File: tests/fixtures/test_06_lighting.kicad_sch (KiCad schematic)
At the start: 2 parts

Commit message: updated test 06 fixtures with LocLoad field
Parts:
- L1: CInfo |(0,0,100)L2.4 -> (none); LocLoad (none) -> (0,0,100)L2.4
- L2: CInfo |(0,0,-100)L2.4 -> (none); LocLoad (none) -> (0,0,-100)L2.4
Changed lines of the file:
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@@
 			)
 		)
-		(property "CInfo" "|(0,0,-100)L2.4"
+		(property "LocLoad" "(0,0,-100)L2.4"
 			(at 45.72 74.93 0)
 			(effects
@@
 			)
 		)
-		(property "CInfo" "|(0,0,10)G"
+		(property "LocLoad" "(0,0,10)G"
 			(at 62.23 74.93 0)
 			(effects
@@
 			)
 		)
-		(property "CInfo" "|(0,0,100)L2.4"
+		(property "LocLoad" "(0,0,100)L2.4"
 			(at 46.99 36.83 0)
 			(effects
@@
 			)
 		)
-		(property "CInfo" "|(0,0,10)G"
-			(at 63.5 36.83 0)
-			(effects
+		(property "LocLoad" "(0,0,10)G"
+			(at 63.5 36.83 0)
+			(effects

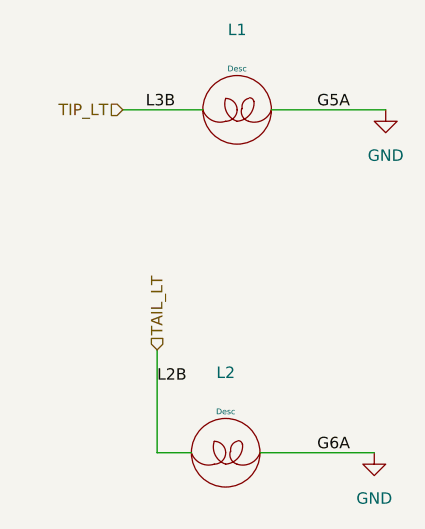
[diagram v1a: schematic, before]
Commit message: updated test_06 and added test_06 avionics. added "A" avionics to circuit types
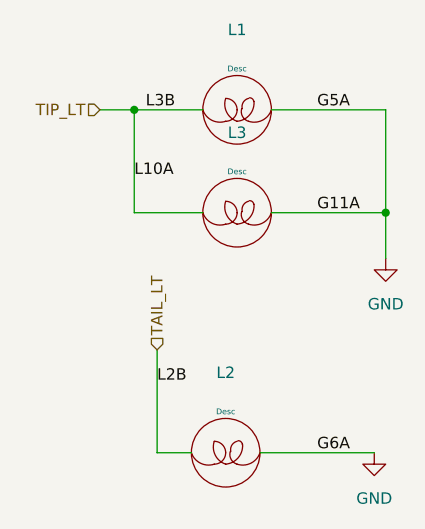
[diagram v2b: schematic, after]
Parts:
- added L3: ~, symbol AeroElectricConnectionSymbols:Lamp
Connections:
- net GND: now also L3.2 (Out)
- net TIP_LT: now also L3.1 (In)
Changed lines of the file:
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@@
 	(generator_version "9.0")
 	(paper "A4")
+	(junction
+		(at 35.56 36.83)
+		(diameter 0)
+		(color 0 0 0 0)
+	)
+	(junction
+		(at 63.5 48.26)
+		(diameter 0)
+		(color 0 0 0 0)
+	)
 	(wire
 		(pts
@@
 	(wire
 		(pts
+			(xy 35.56 48.26) (xy 43.18 48.26)
+		)
+		(stroke
+			(width 0)
+			(type default)
+		)
+	)
+	(wire
+		(pts
+			(xy 63.5 36.83) (xy 50.8 36.83)
+		)
+		(stroke
+			(width 0)
+			(type default)
+		)
+	)
+	(wire
+		(pts
 			(xy 38.1 63.5) (xy 38.1 74.93)
 		)
@@
 	(wire
 		(pts
-			(xy 34.29 36.83) (xy 43.18 36.83)
+			(xy 35.56 36.83) (xy 35.56 48.26)
+		)
+		(stroke
+			(width 0)
+			(type default)
+		)
+	)
+	(wire
+		(pts
+			(xy 63.5 53.34) (xy 63.5 48.26)
+		)
+		(stroke
+			(width 0)
+			(type default)
+		)
+	)
+	(wire
+		(pts
+			(xy 31.75 36.83) (xy 35.56 36.83)
+		)
+		(stroke
+			(width 0)
+			(type default)
+		)
+	)
+	(wire
+		(pts
+			(xy 50.8 48.26) (xy 63.5 48.26)
 		)
 		(stroke
@@
 	(wire
 		(pts
-			(xy 50.8 36.83) (xy 63.5 36.83)
-		)
-		(stroke
-			(width 0)
-			(type default)
+			(xy 35.56 36.83) (xy 43.18 36.83)
+		)
+		(stroke
+			(width 0)
+			(type default)
+		)
+	)
+	(wire
+		(pts
+			(xy 63.5 48.26) (xy 63.5 36.83)
+		)
+		(stroke
+			(width 0)
+			(type default)
+		)
+	)
+	(label "L10A"
+		(at 35.56 44.45 0)
+		(effects
+			(font
+				(size 1.27 1.27)
+			)
+			(justify left bottom)
 		)
 	)
@@
 		)
 	)
+	(label "G11A"
+		(at 55.88 48.26 0)
+		(effects
+			(font
+				(size 1.27 1.27)
+			)
+			(justify left bottom)
+		)
+	)
 	(label "L3B"
 		(at 36.83 36.83 0)
@@
 	(hierarchical_label "TIP_LT"
 		(shape input)
-		(at 34.29 36.83 180)
+		(at 31.75 36.83 180)
 		(effects
 			(font
@@
 	)
 	(symbol
+		(lib_id "AeroElectricConnectionSymbols:Lamp")
+		(at 46.99 48.26 0)
+		(unit 1)
+		(exclude_from_sim no)
+		(in_bom yes)
+		(on_board yes)
+		(dnp no)
+		(fields_autoplaced yes)
+		(property "Reference" "L3"
+			(at 46.99 39.37 0)
+			(effects
+				(font
+					(size 1.27 1.27)
+				)
+			)
+		)
+		(property "Value" "~"
+			(at 46.99 41.91 0)
+			(effects
+				(font
+					(size 1.27 1.27)
+				)
+			)
+		)
+		(property "Footprint" ""
+			(at 46.99 48.26 90)
+			(effects
+				(font
+					(size 1.27 1.27)
+				)
+				(hide yes)
+			)
+		)
+		(property "Datasheet" ""
+			(at 46.99 48.26 90)
+			(effects
+				(font
+					(size 1.27 1.27)
+				)
+				(hide yes)
+			)
+		)
+		(property "Description" "Desc"
+			(at 46.99 43.688 0)
+			(do_not_autoplace yes)
+			(effects
+				(font
+					(size 0.635 0.635)
+				)
+			)
+		)
+		(property "LocLoad" "(0,0,100)L2.4"
+			(at 46.99 48.26 0)
+			(effects
+				(font
+					(size 1.27 1.27)
+				)
+				(hide yes)
+			)
+		)
+		(pin "2"
+		)
+		(pin "1"
+		)
+		(instances
+			(project "test_06_fixture"
+				(path "/6f32b1c6-d0dc-4a69-b565-c121d7833096/b1093350-cedd-46df-81c4-dadfdf2715f8"
+					(reference "L3")
+					(unit 1)
+				)
+			)
+		)
+	)
+	(symbol
 		(lib_id "power:GND")
 		(at 62.23 74.93 0)
@@
 	(symbol
 		(lib_id "power:GND")
-		(at 63.5 36.83 0)
+		(at 63.5 53.34 0)
 		(unit 1)
 		(exclude_from_sim no)
@@
 		(fields_autoplaced yes)
 		(property "Reference" "#PWR01"
-			(at 63.5 43.18 0)
+			(at 63.5 59.69 0)
 			(effects
 				(font
@@
 		)
 		(property "Value" "GND"
-			(at 63.5 41.91 0)
+			(at 63.5 58.42 0)
 			(effects
 				(font
@@
 		)
 		(property "Footprint" ""
-			(at 63.5 36.83 0)
+			(at 63.5 53.34 0)
 			(effects
 				(font
@@
 		)
 		(property "Datasheet" ""
-			(at 63.5 36.83 0)
+			(at 63.5 53.34 0)
 			(effects
 				(font
@@
 		)
 		(property "Description" "Power symbol creates a global label with name \"GND\" , ground"
-			(at 63.5 36.83 0)
+			(at 63.5 53.34 0)
 			(effects
 				(font
@@
 		)
 		(property "LocLoad" "(0,0,10)G"
-			(at 63.5 36.83 0)
-			(effects
-				(font
+			(at 63.5 53.34 0)
+			(effects
+				(font
